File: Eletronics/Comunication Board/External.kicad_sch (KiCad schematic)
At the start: 7 parts, among them J2 Conn_01x10_Female

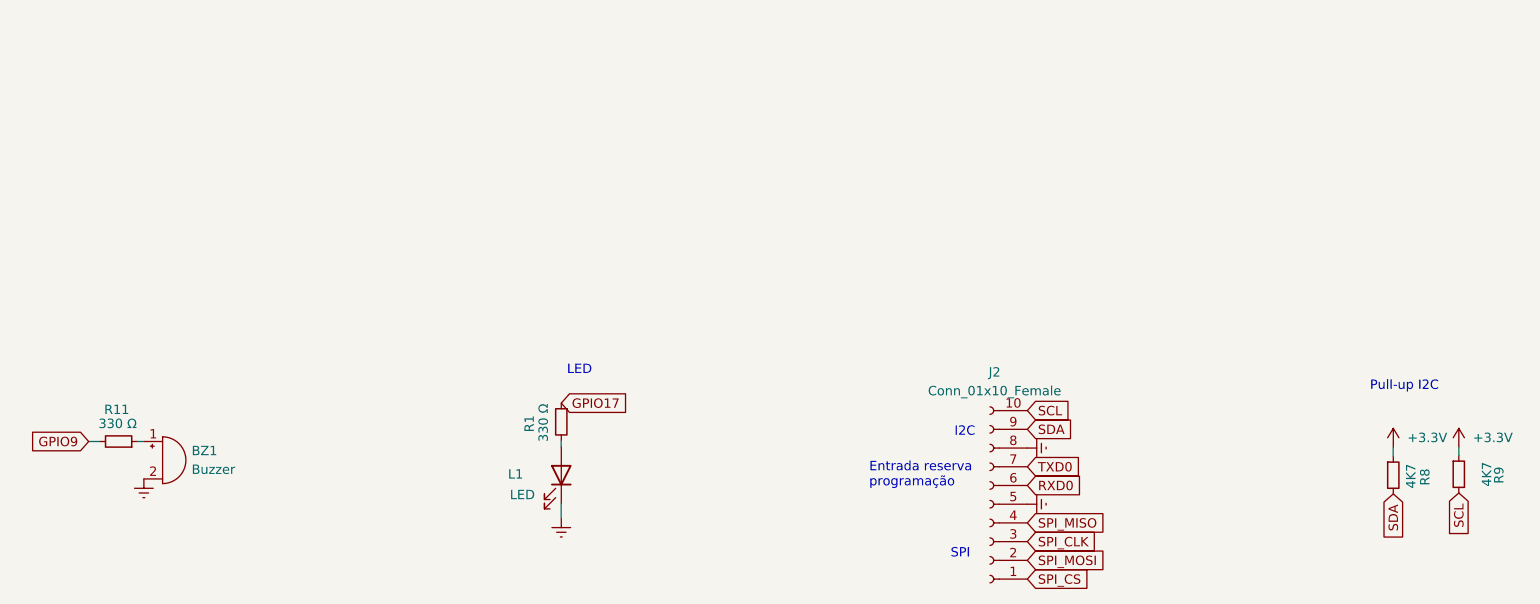
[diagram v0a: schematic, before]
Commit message: Revisão com alterações apontadas no esquemático
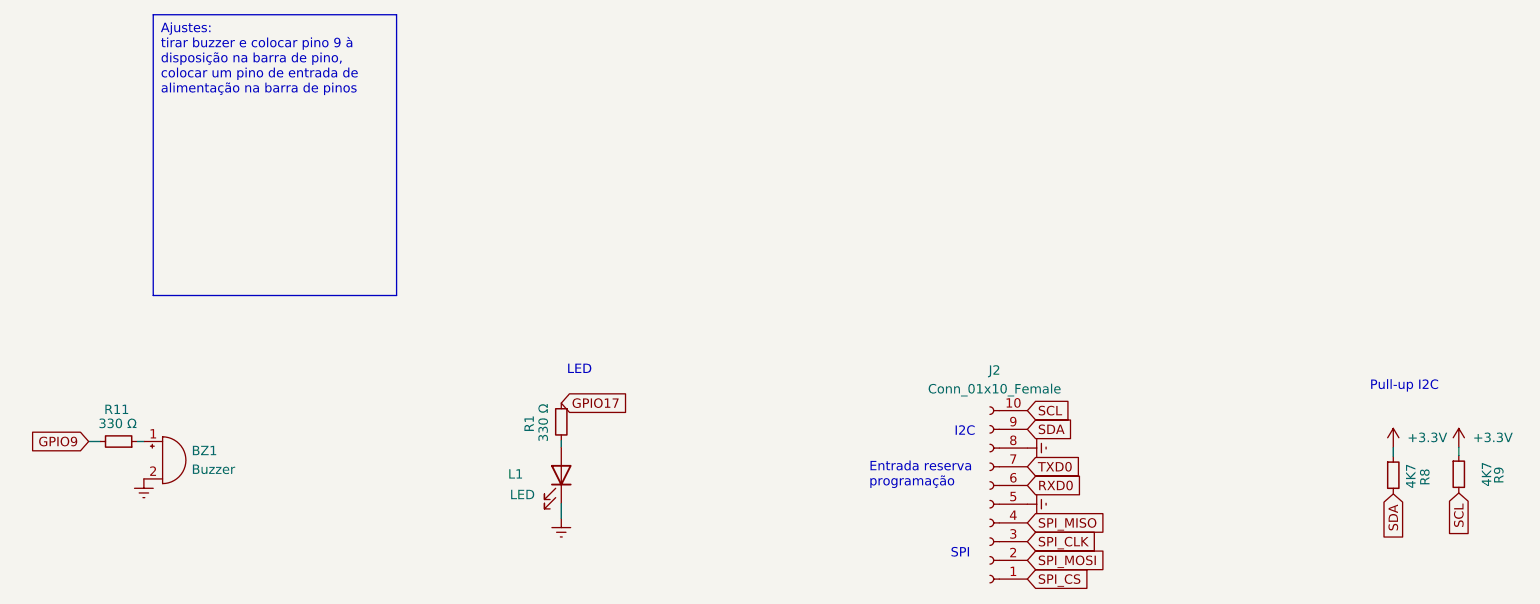
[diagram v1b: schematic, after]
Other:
- company: (none) -> Project Neon
- title: (none) -> Placa de comunicação
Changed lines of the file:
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@@
 	(generator_version "8.0")
 	(paper "A4")
+	(title_block
+		(title "Placa de comunicação")
+		(date "2024-05-04")
+		(rev "0")
+		(company "Project Neon")
+		(comment 1 "Autor: Leticia Martins")
+		(comment 2 "Revisão: Marcus Holanda")
+		(comment 3 "Documento com alterações necessárias, não é um docuemnto final")
+	)
 	(wire
 		(pts
@@
 			(width 0)
 			(type default)
+		)
+	)
+	(text_box "Ajustes:\ntirar buzzer e colocar pino 9 à disposição na barra de pino,\ncolocar um pino de entrada de alimentação na barra de pinos"
+		(exclude_from_sim no)
+		(at 71.12 26.67 0)
+		(size 33.02 38.1)
+		(stroke
+			(width 0)
+			(type default)
+		)
+		(fill
+			(type none)
+		)
+		(effects
+			(font
+				(size 1.27 1.27)
+			)
+			(justify left top)
 		)
 	)
@@
 		(fields_autoplaced yes)
 		(property "Reference" "J2"
-			(at 185.293 75.184 0)
+			(at 185.293 74.93 0)
 			(effects
 				(font
@@
 		)
 		(property "Value" "Conn_01x10_Female"
-			(at 185.293 77.724 0)
-			(effects
-				(font
+			(at 185.293 77.47 0)
+			(effects
+				(font
